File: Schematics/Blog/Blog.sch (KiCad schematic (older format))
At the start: 1 part, among them U1 74HC00

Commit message: Started working on next article
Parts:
- added unit 3 of U1
- added U2: 74HC04, symbol 74xx:74HC04
- added U3: 74HC32, symbol 74xx:74LS32
- added U4: 74HC08, symbol 74xx:74LS08
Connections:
- net PHI2: now also U1.13, U1.9, U2.3; no longer U1.10
- net RDN: now also U1.8, U3.3; no longer U1.6, U1.9
- net R~W: now also U1.10, U2.1
- net WRN: now also U1.11; no longer U1.8
- new net: U1.12, U1.6
- new net: U2.2, U3.1
- new net: U3.2, U4.3
- new net: U2.4, U4.1
- new net RDY: U4.2
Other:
- moved on the sheet: U1B
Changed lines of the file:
@@
 L 74xx:74HC00 U1
 U 2 1 5FE31002
-P 2550 1850
-F 0 "U1" H 2550 2175 50  0000 C CNN
-F 1 "74HC00" H 2550 2084 50  0000 C CNN
-F 2 "" H 2550 1850 50  0001 C CNN
-F 3 "http://www.ti.com/lit/gpn/sn74hc00" H 2550 1850 50  0001 C CNN
-	2    2550 1850
+P 2550 2300
+F 0 "U1" H 2550 2625 50  0000 C CNN
+F 1 "74HC00" H 2550 2534 50  0000 C CNN
+F 2 "" H 2550 2300 50  0001 C CNN
+F 3 "http://www.ti.com/lit/gpn/sn74hc00" H 2550 2300 50  0001 C CNN
+	2    2550 2300
 	1    0    0    -1
 $EndComp
-Text GLabel 2050 1850 0    50   Input ~ 0
+Text GLabel 2050 2300 0    50   Input ~ 0
 R~W
 Wire Wire Line
-	2050 1850 2150 1850
+	2050 2300 2150 2300
 Wire Wire Line
-	2150 1850 2150 1950
+	2150 2300 2150 2400
 Wire Wire Line
-	2150 1950 2250 1950
+	2150 2400 2250 2400
 Wire Wire Line
-	2150 1850 2150 1750
+	2150 2300 2150 2200
 Wire Wire Line
-	2150 1750 2250 1750
-Connection ~ 2150 1850
-Text GLabel 3750 1850 2    50   Output ~ 0
+	2150 2200 2250 2200
+Connection ~ 2150 2300
+Text GLabel 3750 1750 2    50   Output ~ 0
 RDN
-Wire Wire Line
-	2850 1850 2950 1850
 $Comp
 L 74xx:74HC00 U1
-U 3 1 5FE3C714
-P 3350 2300
-F 0 "U1" H 3350 2625 50  0000 C CNN
-F 1 "74HC00" H 3350 2534 50  0000 C CNN
-F 2 "" H 3350 2300 50  0001 C CNN
-F 3 "http://www.ti.com/lit/gpn/sn74hc00" H 3350 2300 50  0001 C CNN
-	3    3350 2300
+U 4 1 5FE3C714
+P 3350 2400
+F 0 "U1" H 3350 2725 50  0000 C CNN
+F 1 "74HC00" H 3350 2634 50  0000 C CNN
+F 2 "" H 3350 2400 50  0001 C CNN
+F 3 "http://www.ti.com/lit/gpn/sn74hc00" H 3350 2400 50  0001 C CNN
+	4    3350 2400
+	1    0    0    -1
+$EndComp
+Text GLabel 3750 2400 2    50   Output ~ 0
+WRN
+Wire Wire Line
+	3650 2400 3750 2400
+Text GLabel 2050 2500 0    50   Input ~ 0
+PHI2
+Wire Wire Line
+	2050 2500 3050 2500
+$Comp
+L 74xx:74HC00 U1
+U 3 1 5FE4F41A
+P 3350 1750
+F 0 "U1" H 3350 2075 50  0000 C CNN
+F 1 "74HC00" H 3350 1984 50  0000 C CNN
+F 2 "" H 3350 1750 50  0001 C CNN
+F 3 "http://www.ti.com/lit/gpn/sn74hc00" H 3350 1750 50  0001 C CNN
+	3    3350 1750
 	1    0    0    -1
 $EndComp
 Wire Wire Line
-	2950 1850 2950 2200
+	3750 1750 3650 1750
 Wire Wire Line
-	2950 2200 3050 2200
+	2850 2300 3050 2300
 Wire Wire Line
-	2950 1850 3750 1850
-Connection ~ 2950 1850
-Text GLabel 3750 2300 2    50   Output ~ 0
-WRN
-Wire Wire Line
-	3650 2300 3750 2300
-Text GLabel 2050 2400 0    50   Input ~ 0
+	2050 1850 3050 1850
+Text GLabel 2050 1850 0    50   Input ~ 0
+R~W
+Text GLabel 2050 1650 0    50   Input ~ 0
 PHI2
 Wire Wire Line
-	2050 2400 3050 2400
+	2050 1650 3050 1650
+$Comp
+L 74xx:74LS32 U3
+U 1 1 5FE8D741
+P 7200 1900
+F 0 "U3" H 7200 2225 50  0000 C CNN
+F 1 "74HC32" H 7200 2134 50  0000 C CNN
+F 2 "" H 7200 1900 50  0001 C CNN
+F 3 "http://www.ti.com/lit/gpn/sn74LS32" H 7200 1900 50  0001 C CNN
+	1    7200 1900
+	1    0    0    -1
+$EndComp
+$Comp
+L 74xx:74HC04 U2
+U 1 1 5FE93B55
+P 6400 1600
+F 0 "U2" H 6400 1917 50  0000 C CNN
+F 1 "74HC04" H 6400 1826 50  0000 C CNN
+F 2 "" H 6400 1600 50  0001 C CNN
+F 3 "https://assets.nexperia.com/documents/data-sheet/74HC_HCT04.pdf" H 6400 1600 50  0001 C CNN
+	1    6400 1600
+	1    0    0    -1
+$EndComp
+Wire Wire Line
+	6700 1600 6800 1600
+Text GLabel 5300 1600 0    50   Input ~ 0
+R~W
+Wire Wire Line
+	5300 1600 6100 1600
+$Comp
+L 74xx:74HC04 U2
+U 2 1 5FE98581
+P 5700 2100
+F 0 "U2" H 5700 2417 50  0000 C CNN
+F 1 "74HC04" H 5700 2326 50  0000 C CNN
+F 2 "" H 5700 2100 50  0001 C CNN
+F 3 "https://assets.nexperia.com/documents/data-sheet/74HC_HCT04.pdf" H 5700 2100 50  0001 C CNN
+	2    5700 2100
+	1    0    0    -1
+$EndComp
+Text GLabel 5300 2100 0    50   Input ~ 0
+PHI2
+Wire Wire Line
+	5300 2100 5400 2100
+$Comp
+L 74xx:74LS08 U4
+U 1 1 5FE9F846
+P 6400 2200
+F 0 "U4" H 6400 2525 50  0000 C CNN
+F 1 "74HC08" H 6400 2434 50  0000 C CNN
+F 2 "" H 6400 2200 50  0001 C CNN
+F 3 "http://www.ti.com/lit/gpn/sn74LS08" H 6400 2200 50  0001 C CNN
+	1    6400 2200
+	1    0    0    -1
+$EndComp
+Wire Wire Line
+	6000 2100 6100 2100
+Text GLabel 5300 2300 0    50   Input ~ 0
+RDY
+Wire Wire Line
+	5300 2300 6100 2300
+Wire Wire Line
+	6700 2200 6800 2200
+Wire Wire Line
+	6800 2200 6800 2000
+Wire Wire Line
+	6800 2000 6900 2000
+Wire Wire Line
+	6800 1600 6800 1800
+Wire Wire Line
+	6800 1800 6900 1800
+Text GLabel 7600 1900 2    50   Output ~ 0
+RDN
+Wire Wire Line
+	7500 1900 7600 1900
 $EndSCHEMATC

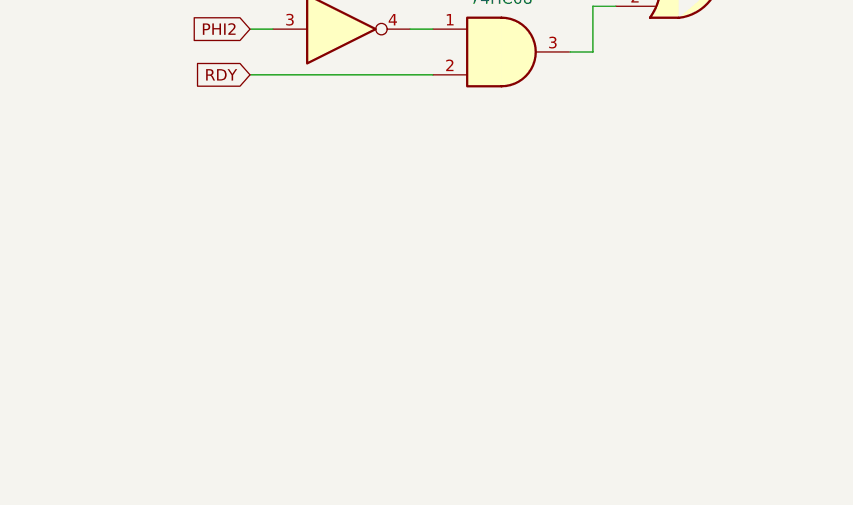
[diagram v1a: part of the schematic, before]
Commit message: Added ws generator schematics
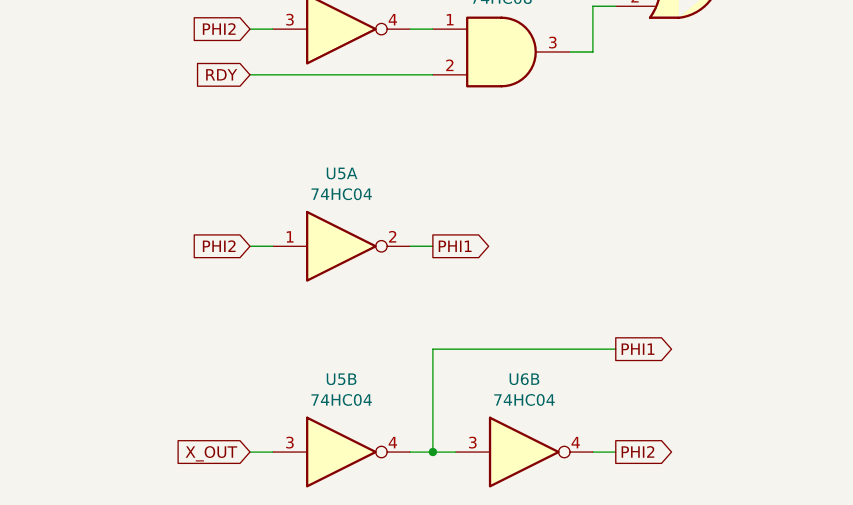
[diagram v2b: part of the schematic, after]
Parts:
- added U5, U6: 74HC04, symbol 74xx:74HC04
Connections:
- net PHI2: now also U5.1, U6.4
- new net PHI1: U5.2, U5.4, U6.3
- new net X_OUT: U5.3
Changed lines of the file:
@@
 Wire Wire Line
 	7500 1900 7600 1900
+$Comp
+L 74xx:74HC04 U5
+U 1 1 60071BB0
+P 5700 3050
+F 0 "U5" H 5700 3367 50  0000 C CNN
+F 1 "74HC04" H 5700 3276 50  0000 C CNN
+F 2 "" H 5700 3050 50  0001 C CNN
+F 3 "https://assets.nexperia.com/documents/data-sheet/74HC_HCT04.pdf" H 5700 3050 50  0001 C CNN
+	1    5700 3050
+	1    0    0    -1
+$EndComp
+Text GLabel 5300 3050 0    50   Input ~ 0
+PHI2
+Wire Wire Line
+	5300 3050 5400 3050
+Text GLabel 6100 3050 2    50   Output ~ 0
+PHI1
+Wire Wire Line
+	6000 3050 6100 3050
+$Comp
+L 74xx:74HC04 U5
+U 2 1 600761BC
+P 5700 3950
+F 0 "U5" H 5700 4267 50  0000 C CNN
+F 1 "74HC04" H 5700 4176 50  0000 C CNN
+F 2 "" H 5700 3950 50  0001 C CNN
+F 3 "https://assets.nexperia.com/documents/data-sheet/74HC_HCT04.pdf" H 5700 3950 50  0001 C CNN
+	2    5700 3950
+	1    0    0    -1
+$EndComp
+$Comp
+L 74xx:74HC04 U6
+U 2 1 60077BC4
+P 6500 3950
+F 0 "U6" H 6500 4267 50  0000 C CNN
+F 1 "74HC04" H 6500 4176 50  0000 C CNN
+F 2 "" H 6500 3950 50  0001 C CNN
+F 3 "https://assets.nexperia.com/documents/data-sheet/74HC_HCT04.pdf" H 6500 3950 50  0001 C CNN
+	2    6500 3950
+	1    0    0    -1
+$EndComp
+Text GLabel 5300 3950 0    50   Input ~ 0
+X_OUT
+Text GLabel 6900 3500 2    50   Output ~ 0
+PHI1
+Text GLabel 6900 3950 2    50   Output ~ 0
+PHI2
+Wire Wire Line
+	6800 3950 6900 3950
+Wire Wire Line
+	6000 3950 6100 3950
+Wire Wire Line
+	6100 3950 6100 3500
+Wire Wire Line
+	6100 3500 6900 3500
+Connection ~ 6100 3950
+Wire Wire Line
+	6100 3950 6200 3950
+Wire Wire Line
+	5300 3950 5400 3950
 $EndSCHEMATC

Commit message: Working on the summary
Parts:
- added U10, U12, U13, U6: 74AC32, symbol 74xx:74LS32
- added U11: 74HC74, symbol 74xx:74HC74
- added U14, U7: 74AC08, symbol 74xx:74LS08
- added U15, U9: 74AC74, symbol 74xx:74HC74
- renumbered U6 to U8
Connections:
- net PHI1: now also U11.3 (C), U15.11 (C), U15.3 (C), U9.11 (C), U9.3 (C)
- net RDY: now also U10.3, U11.2 (D), U6.3, U9.2 (D)
- new net: U10.2, U11.6 (~Q)
- new net: U9.12 (D), U9.5 (Q)
- new net: U7.2, U9.6 (~Q)
- new net: U7.1, U9.8 (~Q)
- new net: U6.2, U7.3
- new net: U14.1, U15.8 (~Q)
- new net: U14.2, U15.6 (~Q)
- new net: U13.2, U14.3
- new net: U15.12 (D), U15.5 (Q)
- new net ~ROM_CS: U10.1, U13.1, U6.1
- no-connect marks 0 -> 13

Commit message: More updates
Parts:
- added unit 2 of U7
- renumbered U13 to U12, U14 to U13, U15 to U14, U12 to U6
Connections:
- net RDY: now also U14.2 (D), U7.6
- net at U13.2, U14.6 (~Q): now also U6.5
- net at U12.3: now also U7.5
- net ~UART_CS: now reaches U6.4
- net at U6.6: now also U7.4
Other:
- moved on the sheet: U6B
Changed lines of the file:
@@
 	2500 6100 2600 6100
-Wire Wire Line
-	1300 5800 1300 7100
 Wire Wire Line
 	1300 7100 1600 7100
 $Comp
-L 74xx:74HC74 U15
+L 74xx:74HC74 U14
 U 2 1 600C4743
 P 2900 7200
-F 0 "U15" H 2900 7681 50  0000 C CNN
+F 0 "U14" H 2900 7681 50  0000 C CNN
 F 1 "74AC74" H 2900 7590 50  0000 C CNN
 F 2 "" H 2900 7200 50  0001 C CNN
@@
 $EndComp
 $Comp
-L 74xx:74HC74 U15
+L 74xx:74HC74 U14
 U 1 1 600C4739
 P 1900 7200
-F 0 "U15" H 1900 7681 50  0000 C CNN
+F 0 "U14" H 1900 7681 50  0000 C CNN
 F 1 "74AC74" H 1900 7590 50  0000 C CNN
 F 2 "" H 1900 7200 50  0001 C CNN
@@
 $EndComp
 $Comp
-L 74xx:74LS32 U13
+L 74xx:74LS32 U12
 U 1 1 600C472F
 P 2900 6200
-F 0 "U13" H 2900 6525 50  0000 C CNN
+F 0 "U12" H 2900 6525 50  0000 C CNN
 F 1 "74AC32" H 2900 6434 50  0000 C CNN
 F 2 "" H 2900 6200 50  0001 C CNN
@@
 $EndComp
 $Comp
-L 74xx:74LS08 U14
+L 74xx:74LS08 U13
 U 1 1 600C4725
 P 1900 6300
-F 0 "U14" H 1900 6625 50  0000 C CNN
+F 0 "U13" H 1900 6625 50  0000 C CNN
 F 1 "74AC08" H 1900 6534 50  0000 C CNN
 F 2 "" H 1900 6300 50  0001 C CNN
@@
 $EndComp
 $Comp
-L 74xx:74LS32 U12
+L 74xx:74LS32 U6
 U 2 1 600FF2B5
-P 2900 5500
-F 0 "U12" H 2900 5825 50  0000 C CNN
-F 1 "74AC32" H 2900 5734 50  0000 C CNN
-F 2 "" H 2900 5500 50  0001 C CNN
-F 3 "http://www.ti.com/lit/gpn/sn74LS32" H 2900 5500 50  0001 C CNN
-	2    2900 5500
+P 2900 5650
+F 0 "U6" H 2900 5975 50  0000 C CNN
+F 1 "74AC32" H 2900 5884 50  0000 C CNN
+F 2 "" H 2900 5650 50  0001 C CNN
+F 3 "http://www.ti.com/lit/gpn/sn74LS32" H 2900 5650 50  0001 C CNN
+	2    2900 5650
 	1    0    0    -1
 $EndComp
+Wire Wire Line
+	1500 6400 1500 5750
+Wire Wire Line
+	1500 5750 2600 5750
+Connection ~ 1500 6400
+Text GLabel 2500 5550 0    50   Input ~ 0
+~UART_CS
+Wire Wire Line
+	2500 5550 2600 5550
+$Comp
+L 74xx:74LS08 U7
+U 2 1 6010D5D4
+P 3700 5750
+F 0 "U7" H 3700 6075 50  0000 C CNN
+F 1 "74AC08" H 3700 5984 50  0000 C CNN
+F 2 "" H 3700 5750 50  0001 C CNN
+F 3 "http://www.ti.com/lit/gpn/sn74LS08" H 3700 5750 50  0001 C CNN
+	2    3700 5750
+	1    0    0    -1
+$EndComp
+Wire Wire Line
+	3200 6200 3300 6200
+Wire Wire Line
+	3300 6200 3300 5850
+Wire Wire Line
+	3300 5850 3400 5850
+Wire Wire Line
+	3200 5650 3400 5650
+Text GLabel 4200 5750 2    50   Output ~ 0
+RDY
+Wire Wire Line
+	4000 5750 4100 5750
+Wire Wire Line
+	4100 5750 4100 5250
+Wire Wire Line
+	4100 5250 1300 5250
+Wire Wire Line
+	1300 5250 1300 7100
+Connection ~ 4100 5750
+Wire Wire Line
+	4100 5750 4200 5750
 $EndSCHEMATC
